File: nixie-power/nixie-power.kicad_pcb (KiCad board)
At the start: 2 copper layers, 48.8 x 48.8 mm, 22 parts, among them CON1 BARREL_JACK, P1 CONN_2, P2 CONN_2, P3 CONN_3, Q1 MOSFET_N, U1 MAX1771

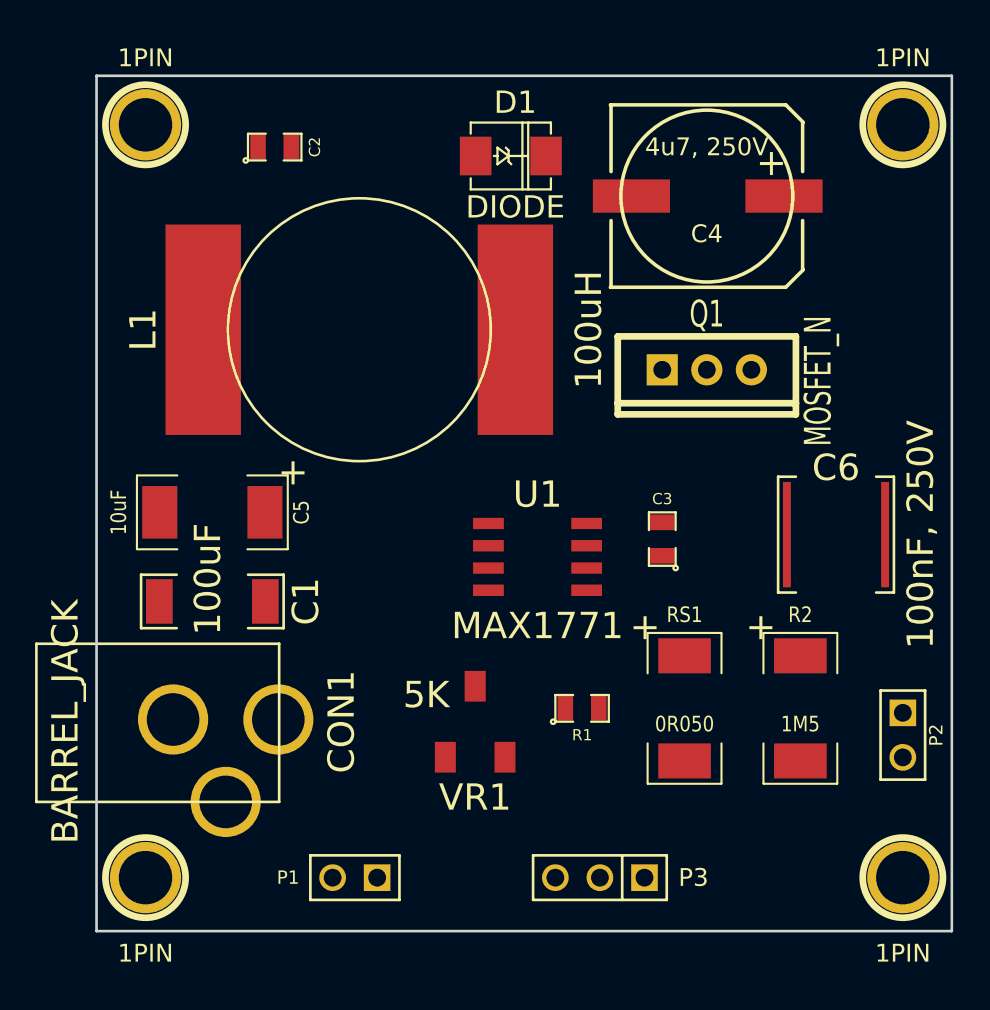
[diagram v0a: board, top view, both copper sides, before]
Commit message: nixie-power: Fix C4 foot print. Tune layout.
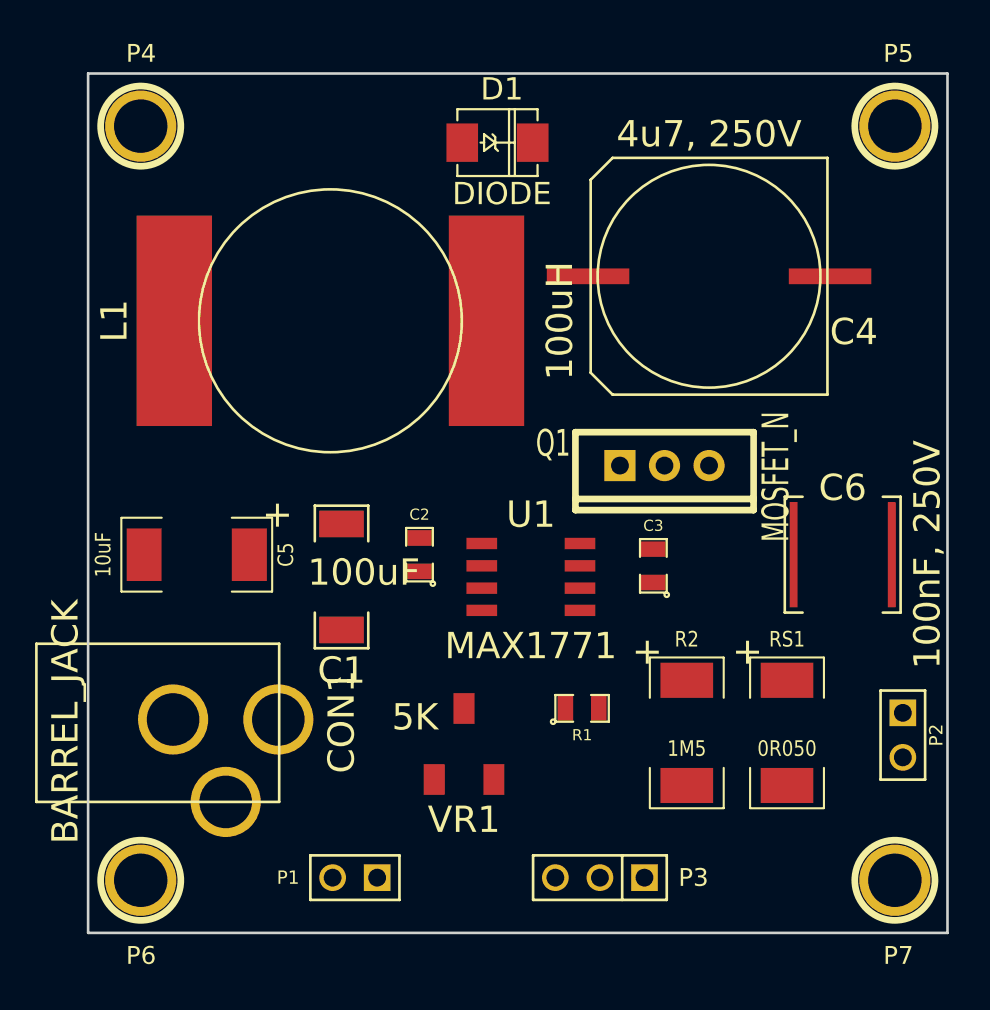
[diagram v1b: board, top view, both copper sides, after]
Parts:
- removed 1PIN (x4): P***, 1pin
- added P4: CONN_1, 1pin, F.Cu at (33.0, 27.0)
- added P5: CONN_1, 1pin, F.Cu at (76.0, 27.0)
- added P6: CONN_1, 1pin, F.Cu at (33.0, 70.0)
- added P7: CONN_1, 1pin, F.Cu at (76.0, 70.0)
- C4: footprint SMDSVP10 -> c_elec_13.5x13.8
- moved C2 24.7 mm to (48.9, 51.4), turned to 90 degrees
- moved C1 7.50 mm to (44.5, 52.7), turned to 90 degrees
- moved R2 6.63 mm to (64.1, 61.6)
- moved RS1 6.01 mm to (69.8, 61.6)
- moved Q1 5.97 mm to (62.9, 46.4)
- moved C4 4.57 mm to (65.4, 35.6)
- moved C5 2.57 mm to (36.2, 51.4)
- moved L1 1.73 mm to (43.8, 38.1)
- moved C3 1.61 mm to (62.2, 52.1)
- moved VR1 1.42 mm to (51.4, 62.2)
- moved C6 1.20 mm to (73.0, 51.4)
- moved U1 1.20 mm to (55.2, 52.7)
- moved D1 1.08 mm to (53.3, 27.9)
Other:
- board size 48.8 x 48.8 mm -> 49 x 49 mm

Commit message: nixie-power: Added initial tracing.
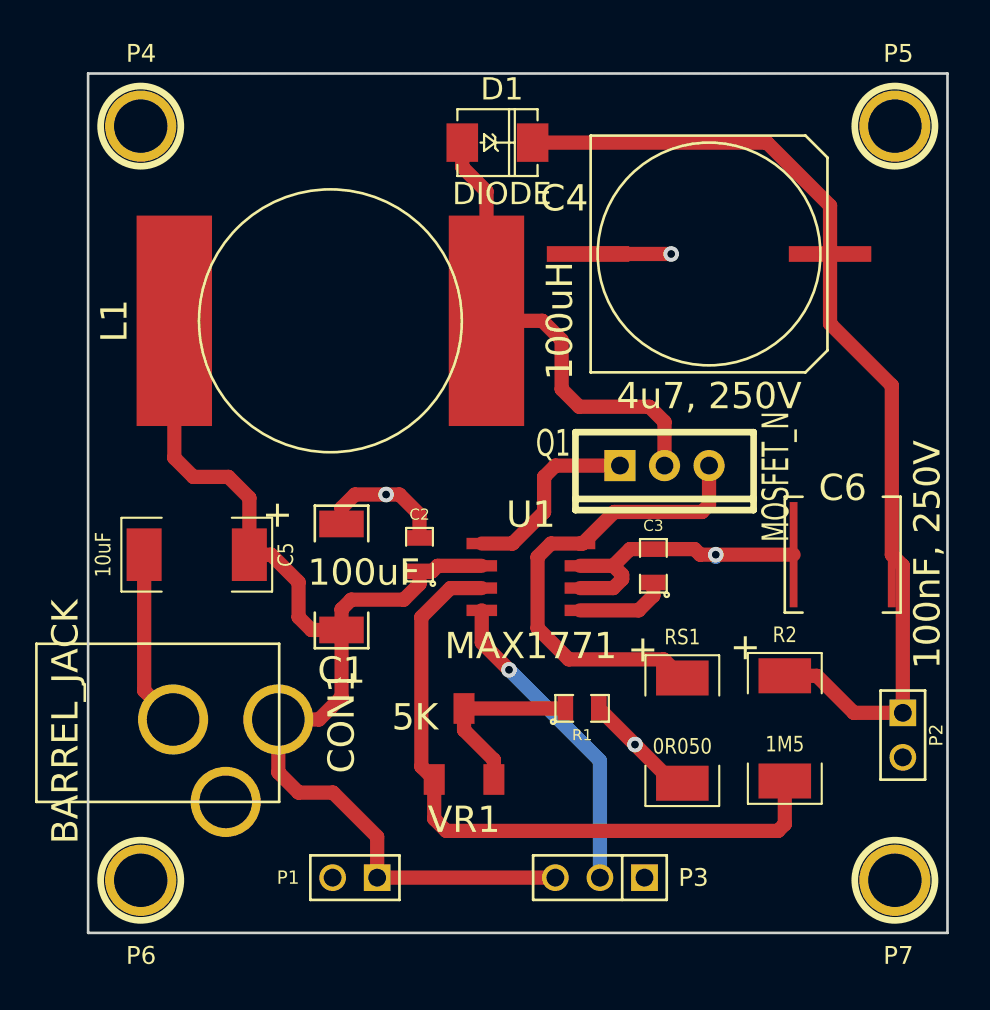
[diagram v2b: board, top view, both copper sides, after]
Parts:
- moved RS1 5.97 mm to (63.9, 61.5)
- moved R2 5.59 mm to (69.7, 61.3)
- moved C4 1.27 mm to (65.4, 34.3), turned to 0 degrees
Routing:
- net N-000003: track 0.00 -> 65.7 mm
- net N-000005: track 0.00 -> 56.7 mm
- net GND: track 0.00 -> 45.3 mm, vias 0 -> 4
- net FB: track 0.00 -> 38.8 mm
- net N-000009: track 0.00 -> 27.4 mm
- net N-000006: track 0.00 -> 26.7 mm
- net N-000008: track 0.00 -> 18.0 mm, vias 0 -> 1
- net N-000004: track 0.00 -> 10.9 mm
- net N-0000011: track 0.00 -> 10.5 mm
- net N-000002: track 0.00 -> 5.28 mm
- added copper zone on B.Cu, net GND
